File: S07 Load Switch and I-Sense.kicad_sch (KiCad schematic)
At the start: 62 parts, among them Q20 BSS138, Q21 BSS138, Q22 BSS138, U10 TLV9002IDSG, U6 TPS22811, U7 TPS22811, U8 TLV9002IDSG, U9 TPS22811

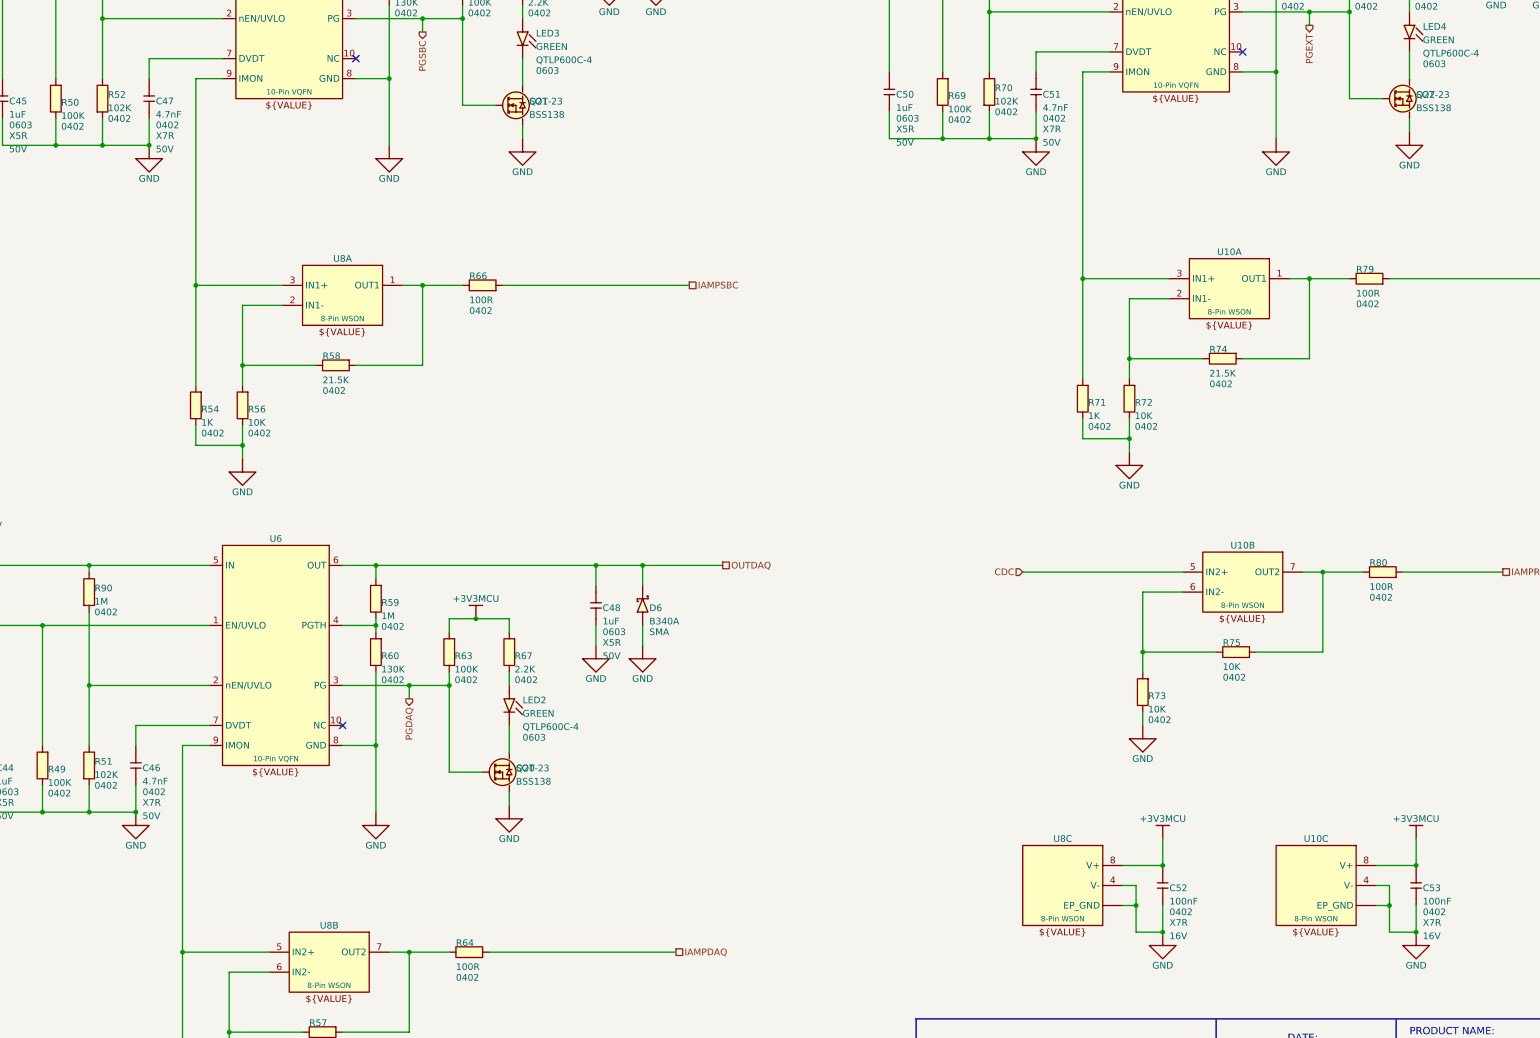
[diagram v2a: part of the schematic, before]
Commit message: BOM consolidation, OVLO divider to 1%, U5 fixes and I2C config option
- Consolidate passives: 1uF 50V to 0603, 100nF to 50V X7R 0402,
  10uF to 50V X7R 1210, 220nF to 0603, 10R to 0402 (100 -> 90 BOM lines)
- TPS22811 OVLO divider 1M/102K 0.1% -> 1M/100K 1% (12.6V min trip)
- U5 LM51772: C30 -> R102 10K to GND (VCC1 disabled), C32 -> 22uF 16V 0805,
  R29 1.9K -> 1.87K to sit inside the CFG4 window
- Add DNP I2C configuration option for U5 (R103-R107) on J3.34/J3.36,
  shared with R97/R98 fallback
- Document all changes in README.md

Co-Authored-By: Claude Opus 5.5 <noreply@anthropic.com>
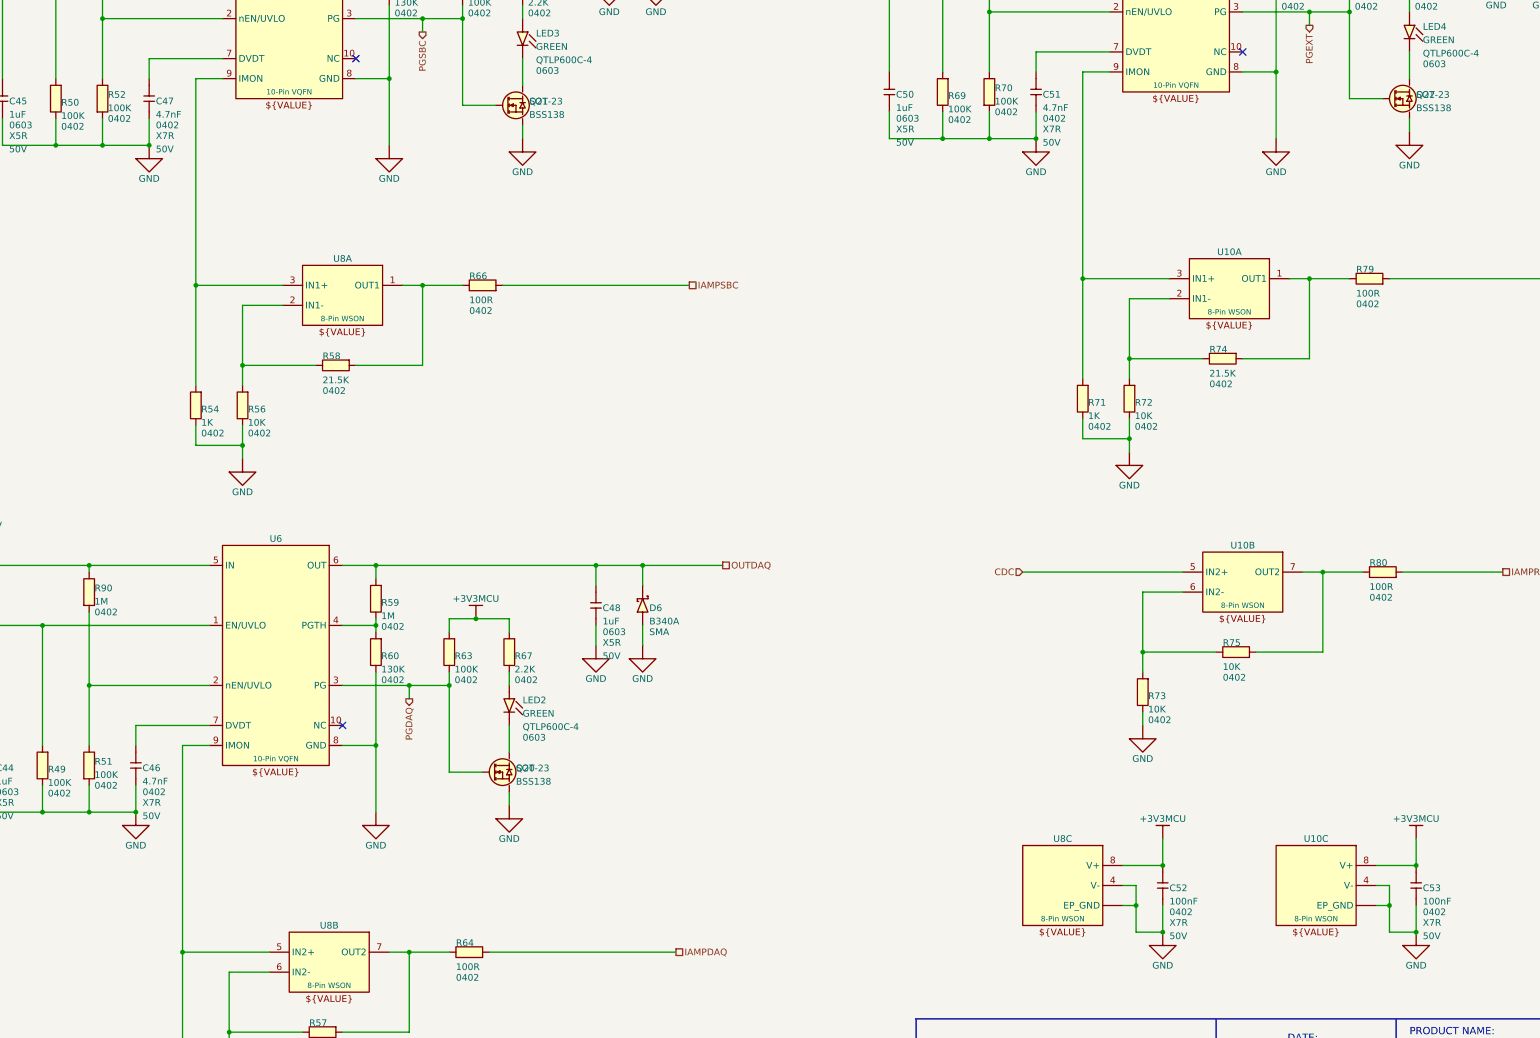
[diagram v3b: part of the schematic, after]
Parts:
- C52, C53: symbol Lattech Systems:Capacitor 100nF 16V X7R 0402 -> Lattech Systems:Capacitor 100nF 50V X7R 0402; MANUFACTURER ? -> Yageo; MANUFACTURER_PN ? -> CC0402KPX7R9BB104; VOLTAGE 16V -> 50V
- R51, R52, R70: value 102K -> 100K; symbol Lattech Systems:Resistor 102K 0.1% 0402 -> Lattech Systems:Resistor 100K 1% 0402; ALTIUM_VALUE 102K -> 100K
- R90, R91, R92: symbol Lattech Systems:Resistor 1M 0.1% 0402 -> Lattech Systems:Resistor 1M 1% 0402
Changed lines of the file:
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@@
 	)
 	(symbol
-		(lib_id "Lattech Systems:Resistor 102K 0.1% 0402")
+		(lib_id "Lattech Systems:Resistor 100K 1% 0402")
 		(at 76.2 85.09 270)
 		(unit 1)
@@
 			)
 		)
-		(property "Value" "102K"
+		(property "Value" "100K"
 			(at 75.184 80.772 90)
 			(hide yes)
@@
 			)
 		)
-		(property "Description" "Resistor 102K 0.1% 0402"
+		(property "Description" "Resistor 100K 1% 0402"
 			(at 76.2 85.09 0)
 			(hide yes)
@@
 			)
 		)
-		(property "ALTIUM_VALUE" "102K"
+		(property "ALTIUM_VALUE" "100K"
 			(at 77.216 87.63 90)
 			(show_name no)
@@
 	)
 	(symbol
-		(lib_id "Lattech Systems:Resistor 102K 0.1% 0402")
+		(lib_id "Lattech Systems:Resistor 100K 1% 0402")
 		(at 73.66 212.09 270)
 		(unit 1)
@@
 			)
 		)
-		(property "Value" "102K"
+		(property "Value" "100K"
 			(at 72.644 207.772 90)
 			(hide yes)
@@
 			)
 		)
-		(property "Description" "Resistor 102K 0.1% 0402"
+		(property "Description" "Resistor 100K 1% 0402"
 			(at 73.66 212.09 0)
 			(hide yes)
@@
 			)
 		)
-		(property "ALTIUM_VALUE" "102K"
+		(property "ALTIUM_VALUE" "100K"
 			(at 74.676 214.63 90)
 			(show_name no)
@@
 	)
 	(symbol
-		(lib_id "Lattech Systems:Resistor 1M 0.1% 0402")
+		(lib_id "Lattech Systems:Resistor 1M 1% 0402")
 		(at 76.2 52.07 270)
 		(unit 1)
@@
 			)
 		)
-		(property "Description" "Resistor 1M 0.1% 0402"
+		(property "Description" "Resistor 1M 1% 0402"
 			(at 76.2 52.07 0)
 			(hide yes)
@@
 	)
 	(symbol
-		(lib_id "Lattech Systems:Resistor 102K 0.1% 0402")
+		(lib_id "Lattech Systems:Resistor 100K 1% 0402")
 		(at 245.11 83.82 270)
 		(unit 1)
@@
 			)
 		)
-		(property "Value" "102K"
+		(property "Value" "100K"
 			(at 244.094 79.502 90)
 			(hide yes)
@@
 			)
 		)
-		(property "Description" "Resistor 102K 0.1% 0402"
+		(property "Description" "Resistor 100K 1% 0402"
 			(at 245.11 83.82 0)
 			(hide yes)
@@
 			)
 		)
-		(property "ALTIUM_VALUE" "102K"
+		(property "ALTIUM_VALUE" "100K"
 			(at 246.126 86.36 90)
 			(show_name no)
@@
 	)
 	(symbol
-		(lib_id "Lattech Systems:Capacitor 100nF 16V X7R 0402")
+		(lib_id "Lattech Systems:Capacitor 100nF 50V X7R 0402")
 		(at 278.13 234.95 90)
 		(unit 1)
@@
 			)
 		)
-		(property "Description" "Capacitor 100nF 16V X7R 0402"
+		(property "Description" "Capacitor 100nF 50V X7R 0402"
 			(at 278.13 234.95 0)
 			(hide yes)
@@
 			)
 		)
-		(property "MANUFACTURER" "?"
+		(property "MANUFACTURER" "Yageo"
 			(at 276.86 230.632 90)
 			(hide yes)
@@
 			)
 		)
-		(property "MANUFACTURER_PN" "?"
+		(property "MANUFACTURER_PN" "CC0402KPX7R9BB104"
 			(at 276.86 230.632 90)
 			(hide yes)
@@
 			)
 		)
-		(property "VOLTAGE" "16V"
+		(property "VOLTAGE" "50V"
 			(at 279.4 243.84 90)
 			(show_name no)
@@
 	)
 	(symbol
-		(lib_id "Lattech Systems:Resistor 1M 0.1% 0402")
+		(lib_id "Lattech Systems:Resistor 1M 1% 0402")
 		(at 245.11 50.8 270)
 		(unit 1)
@@
 			)
 		)
-		(property "Description" "Resistor 1M 0.1% 0402"
+		(property "Description" "Resistor 1M 1% 0402"
 			(at 245.11 50.8 0)
 			(hide yes)
@@
 	)
 	(symbol
-		(lib_id "Lattech Systems:Capacitor 100nF 16V X7R 0402")
+		(lib_id "Lattech Systems:Capacitor 100nF 50V X7R 0402")
 		(at 326.39 234.95 90)
 		(unit 1)
@@
 			)
 		)
-		(property "Description" "Capacitor 100nF 16V X7R 0402"
+		(property "Description" "Capacitor 100nF 50V X7R 0402"
 			(at 326.39 234.95 0)
 			(hide yes)
@@
 			)
 		)
-		(property "MANUFACTURER" "?"
+		(property "MANUFACTURER" "Yageo"
 			(at 325.12 230.632 90)
 			(hide yes)
@@
 			)
 		)
-		(property "MANUFACTURER_PN" "?"
+		(property "MANUFACTURER_PN" "CC0402KPX7R9BB104"
 			(at 325.12 230.632 90)
 			(hide yes)
@@
 			)
 		)
-		(property "VOLTAGE" "16V"
+		(property "VOLTAGE" "50V"
 			(at 327.66 243.84 90)
 			(show_name no)
@@
 	)
 	(symbol
-		(lib_id "Lattech Systems:Resistor 1M 0.1% 0402")
+		(lib_id "Lattech Systems:Resistor 1M 1% 0402")
 		(at 73.66 179.07 270)
 		(unit 1)
@@
 			)
 		)
-		(property "Description" "Resistor 1M 0.1% 0402"
+		(property "Description" "Resistor 1M 1% 0402"
 			(at 73.66 179.07 0)
 			(hide yes)

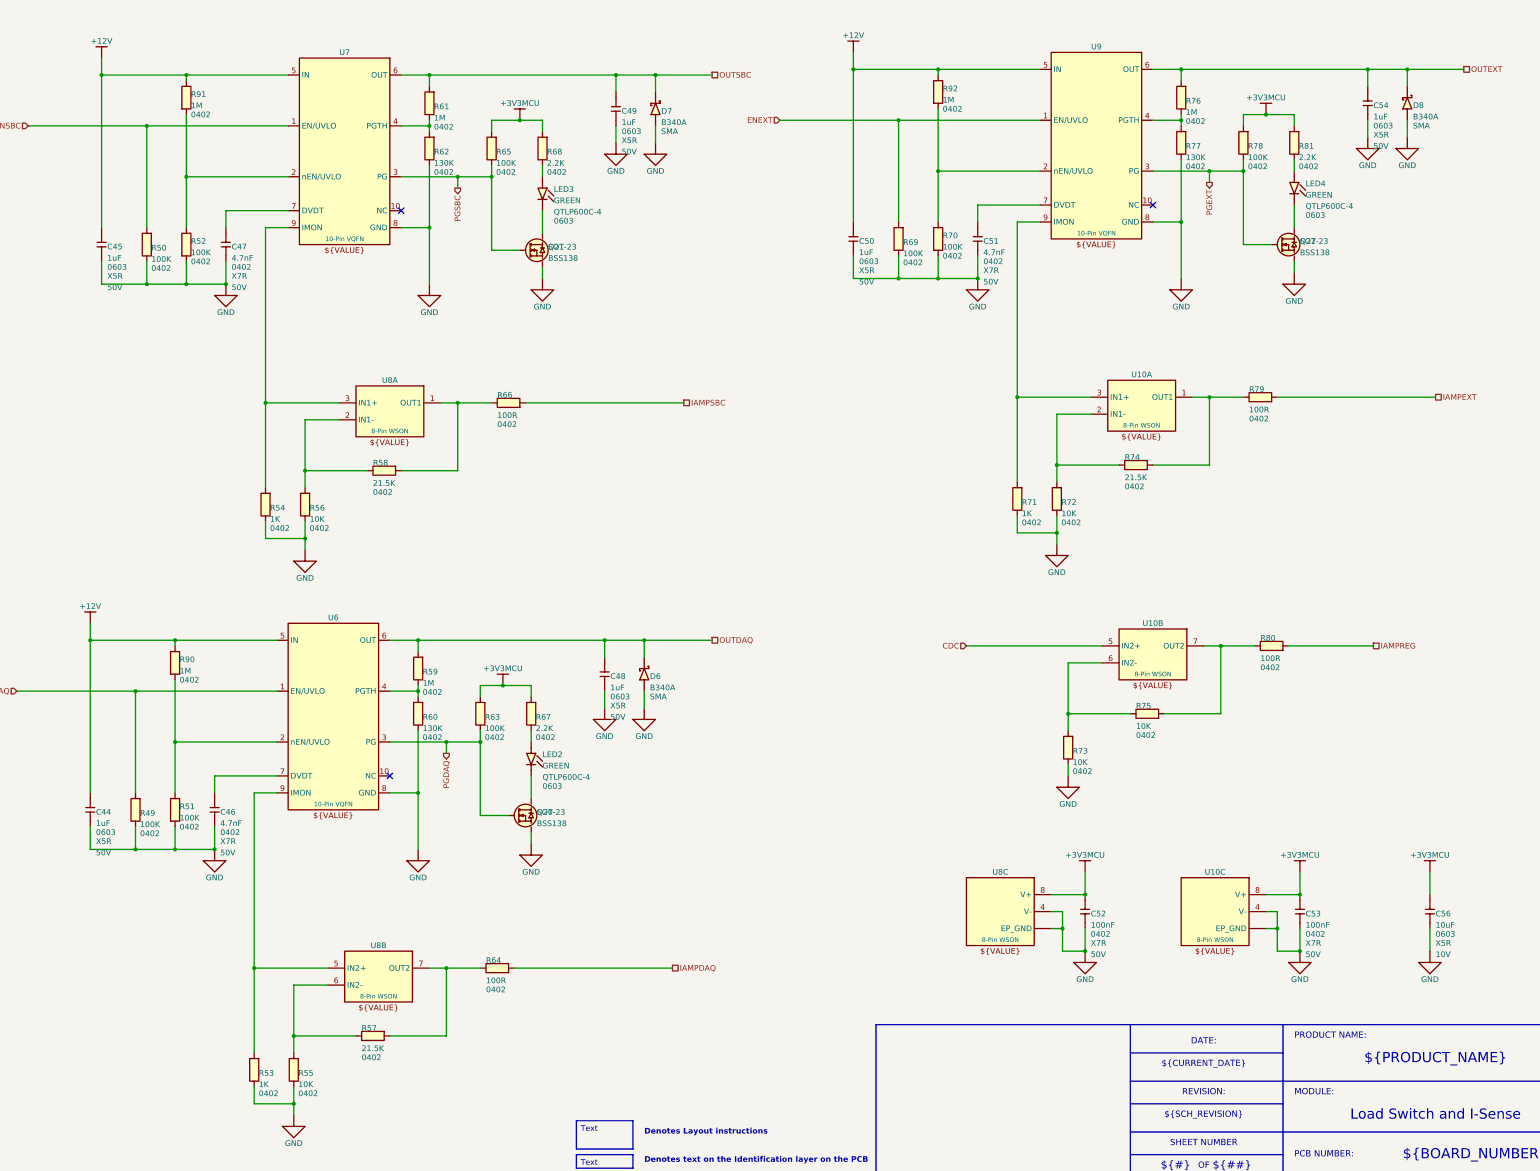
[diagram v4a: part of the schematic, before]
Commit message: Final-revision value changes and standard R/C symbols
Values (schematic and PCB):
- C2 100uF -> 82uF, matching the ordered 35SVPF82M
- C46, C47, C51 (TPS22811 DVDT) 4.7nF -> 1.8nF CC0402KRX7R9BB182 for a
  shorter output ramp
- R24-R27 10R -> 0R; D9, D10 and R36 DNP
- R14 0.01R -> 0.012R PA2512FKF7W0R012E

Symbols:
- All 160 resistors and capacitors now use Device:R, Device:C and
  Device:C_Polarized; the 76 per-value R/C symbols are removed from the
  project library. Connectivity is unchanged (netlist compared).
- Value is now the displayed field instead of ALTIUM_VALUE, which had left
  R1, C39 and R54 showing their old values. ALTIUM_VALUE synced with Value
  on R1, C39, R54, D1, Q1, Q3 and L1.
- Net-(C40-+) is now Net-(U5-ISNSP); renamed on the PCB and in the
  PWR 15A net class pattern.

Co-Authored-By: Claude Opus 5.5 <noreply@anthropic.com>
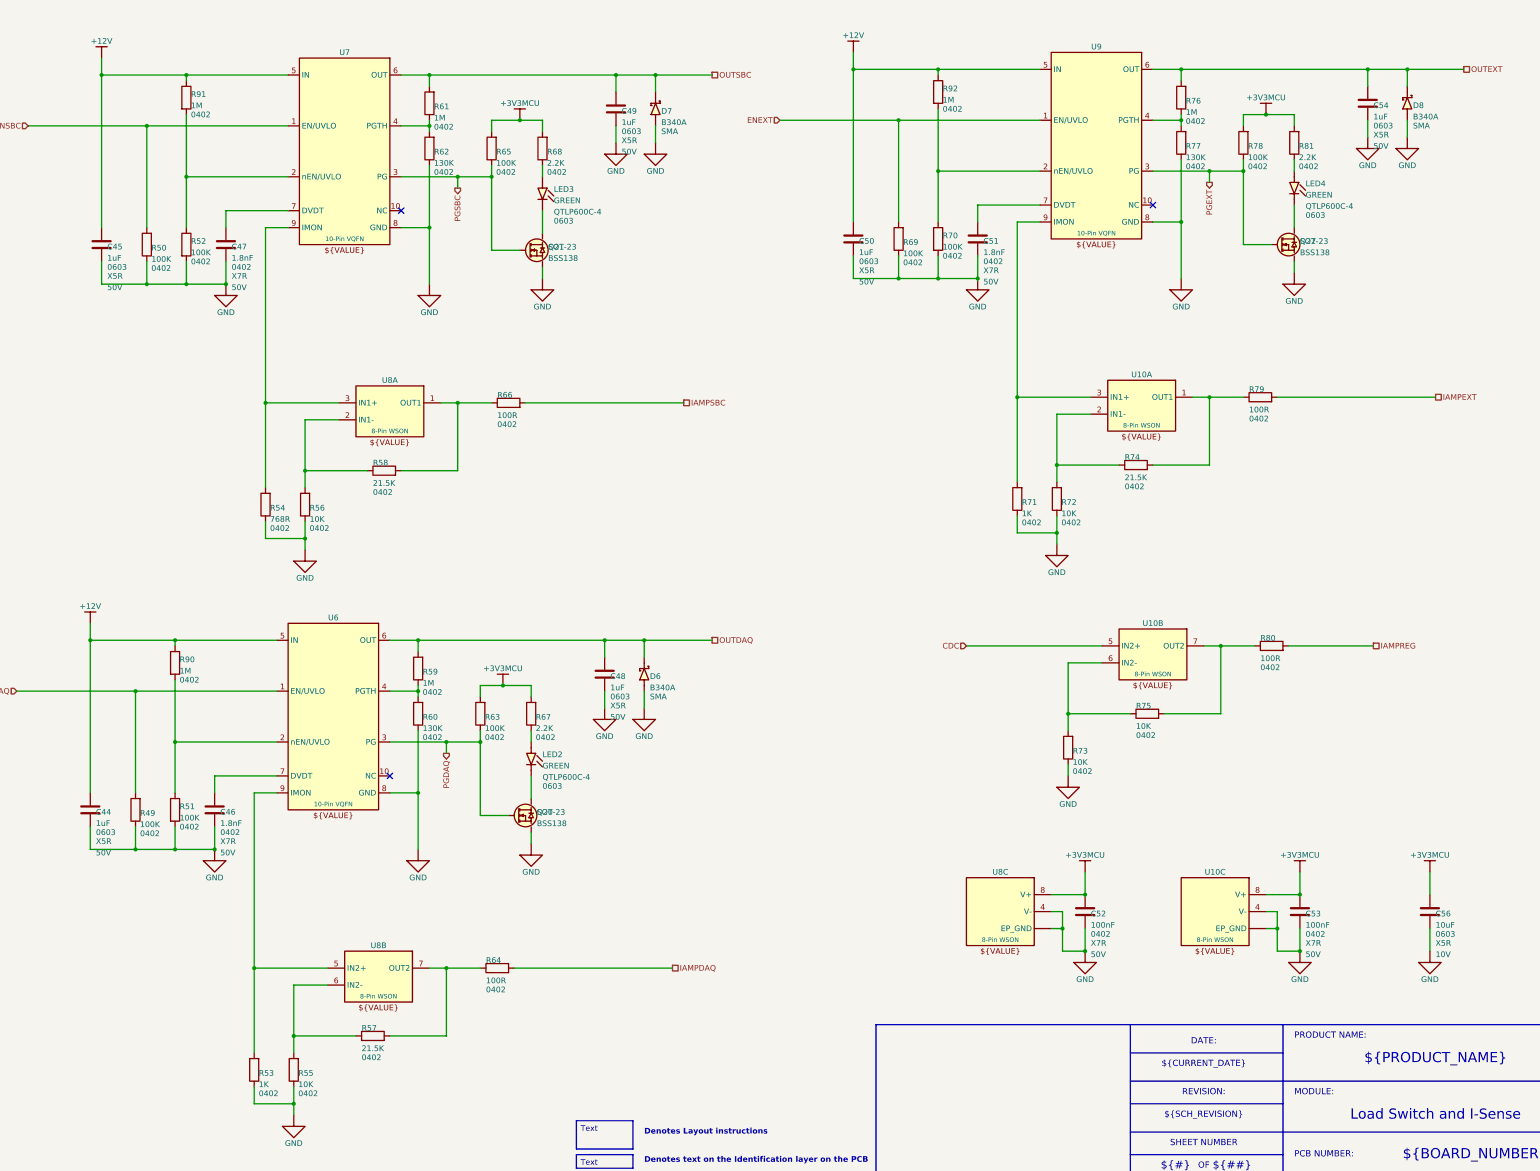
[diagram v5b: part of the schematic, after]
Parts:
- C44, C45, C48, C49, C50, C54: symbol Lattech Systems:Capacitor 1uF 50V X5R 0603 -> Device:C
- C46, C47, C51: value 4.7nF -> 1.8nF; symbol Lattech Systems:Capacitor 4.7nF 50V X7R 0402 -> Device:C; ALTIUM_VALUE 4.7nF -> 1.8nF; MANUFACTURER (none) -> Yageo; MANUFACTURER_PN (none) -> CC0402KRX7R9BB182
- C52, C53: symbol Lattech Systems:Capacitor 100nF 50V X7R 0402 -> Device:C
- C56: symbol Lattech Systems:Capacitor 10uF 10V X5R 0603 -> Device:C
- R49, R50, R51, R52, R63, R65, R69, R70, R78: symbol Lattech Systems:Resistor 100K 1% 0402 -> Device:R
- R53, R71: symbol Lattech Systems:Resistor 1K 1% 0402 -> Device:R
- R54: symbol Lattech Systems:Resistor 768R 1% 0402 -> Device:R; ALTIUM_VALUE 1K -> 768R
- R55, R56, R72, R73, R75: symbol Lattech Systems:Resistor 10K 1% 0402 -> Device:R
- R57, R58, R74: symbol Lattech Systems:Resistor 21.5K 1% 0402 -> Device:R
- R59, R61, R76, R90, R91, R92: symbol Lattech Systems:Resistor 1M 1% 0402 -> Device:R
- R60, R62, R77: symbol Lattech Systems:Resistor 130K 1% 0402 -> Device:R
- R64, R66, R79, R80: symbol Lattech Systems:Resistor 100R 1% 0402 -> Device:R
- R67, R68, R81: symbol Lattech Systems:Resistor 2.2K 1% 0402 -> Device:R
